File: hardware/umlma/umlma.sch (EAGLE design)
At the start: 13 parts, among them IC1 TINY25, J1 AVRISP6_TP

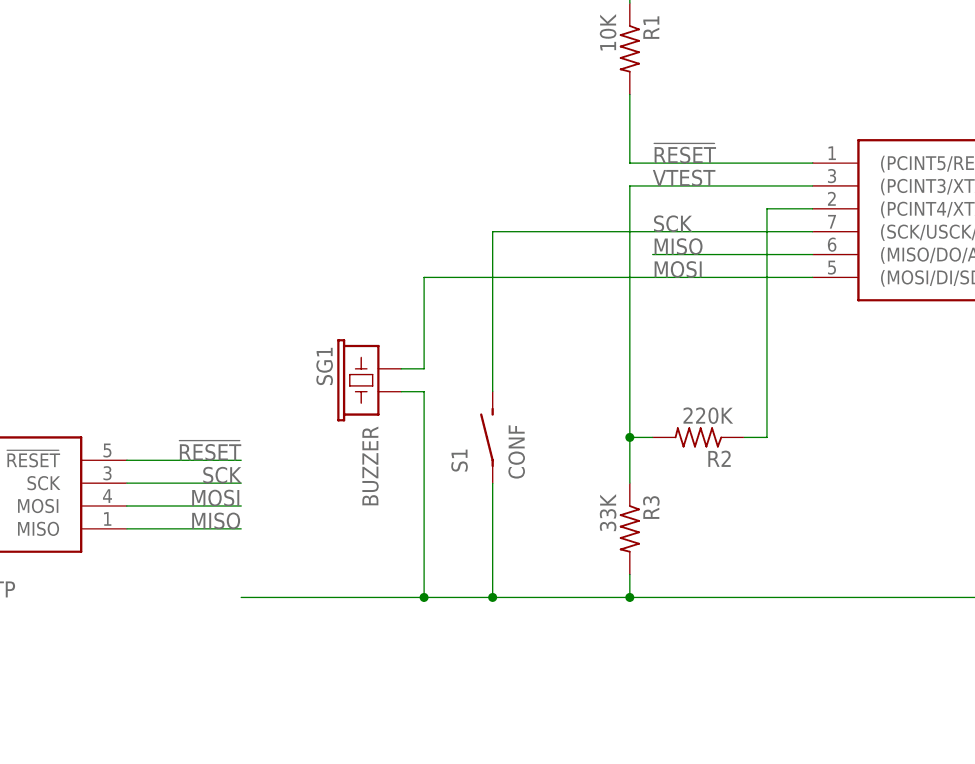
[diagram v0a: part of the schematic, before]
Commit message: revise mcu pin assignments
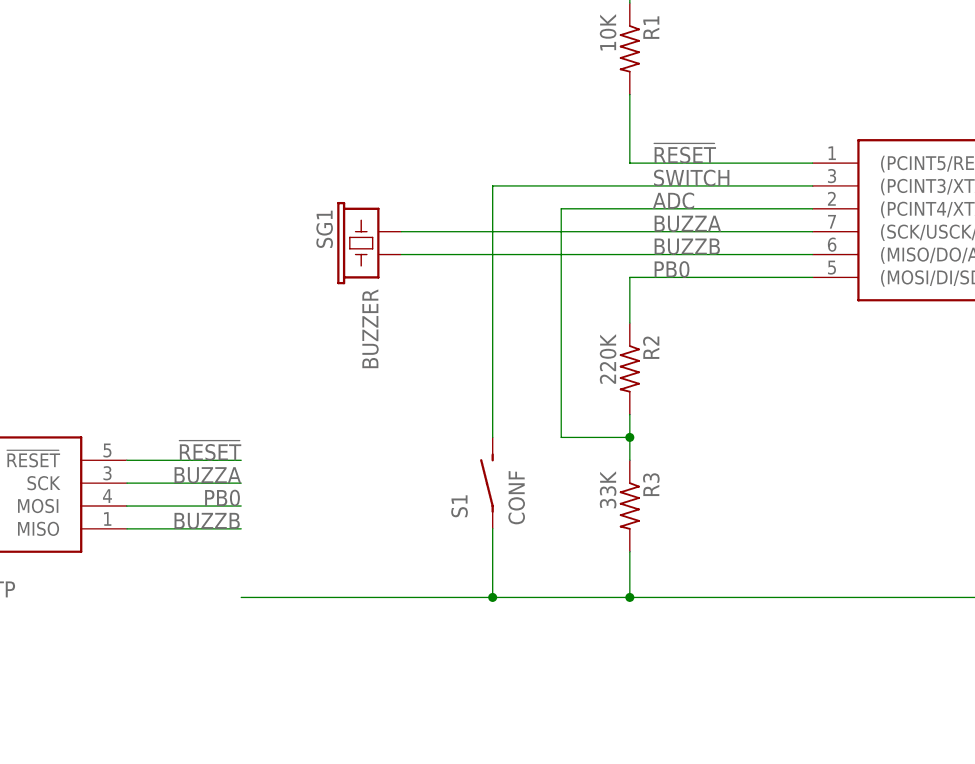
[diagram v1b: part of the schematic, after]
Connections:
- removed net MISO: IC1.(MISO/DO/AIN1/OC0B/OC1A/PCINT1)PB1, J1.MISO
- removed net MOSI: IC1.(MOSI/DI/SDA/AIN0/OC0A/OC1A/AREF/PCINT0)PB0, J1.MOSI, SG1.1
- removed net N$5: IC1.(PCINT4/XTAL2/CLKO/OC1B/ADC2)PB3, R2.1
- removed net SCK: IC1.(SCK/USCK/SCL/ADC1/T0/INT0/PCINT2)PB2, J1.SCK, S1.S
- removed net VTEST: IC1.(PCINT3/XTAL1/CLKI/OC1B/ADC3)PB4, R2.2, R3.1
- new net ADC: IC1.(PCINT4/XTAL2/CLKO/OC1B/ADC2)PB3, R2.2, R3.1
- new net BUZZA: IC1.(SCK/USCK/SCL/ADC1/T0/INT0/PCINT2)PB2, J1.SCK, SG1.1
- new net BUZZB: IC1.(MISO/DO/AIN1/OC0B/OC1A/PCINT1)PB1, J1.MISO, SG1.2
- new net PB0: IC1.(MOSI/DI/SDA/AIN0/OC0A/OC1A/AREF/PCINT0)PB0, J1.MOSI, R2.1
- new net SWITCH: IC1.(PCINT3/XTAL1/CLKI/OC1B/ADC3)PB4, S1.S
- net GND: no longer SG1.2
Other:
- moved on the sheet: R2, R3, S1, SG1
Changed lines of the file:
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@@
 <attribute name="BOM" value="EXCLUDE"/>
-</part>
-<part name="R2" library="rcl" deviceset="R-US_" device="R0603" value="220K">
-<attribute name="PARTNO" value="ERJ-3GEYJ102V"/>
 </part>
 <part name="R3" library="rcl" deviceset="R-US_" device="R0603" value="33K">
@@
 <part name="PAD4" library="wirepad" deviceset="WIREPAD" device="1,6/0,8" value="VCC">
 <attribute name="BOM" value="EXCLUDE"/>
+</part>
+<part name="R2" library="rcl" deviceset="R-US_" device="R0603" value="220K">
+<attribute name="PARTNO" value="ERJ-3GEYJ102V"/>
 </part>
 </parts>
@@
 <instance part="SUPPLY1" gate="GND" x="139.7" y="50.8"/>
 <instance part="P+1" gate="VCC" x="137.16" y="134.62"/>
-<instance part="SG1" gate="G$1" x="71.12" y="83.82" rot="MR270">
-<attribute name="PARTNO" x="71.12" y="83.82" size="1.778" layer="96" rot="MR270" display="off"/>
+<instance part="SG1" gate="G$1" x="71.12" y="99.06" rot="MR270">
+<attribute name="PARTNO" x="71.12" y="99.06" size="1.778" layer="96" rot="MR270" display="off"/>
 </instance>
 <instance part="PAD1" gate="G$1" x="223.52" y="106.68" rot="R180">
@@
 <attribute name="BOM" x="223.52" y="99.06" size="1.778" layer="96" display="off"/>
 </instance>
-<instance part="R2" gate="G$1" x="106.68" y="76.2" rot="R180">
-<attribute name="PARTNO" x="106.68" y="76.2" size="1.778" layer="96" rot="R270" display="off"/>
-</instance>
-<instance part="R3" gate="G$1" x="99.06" y="66.04" rot="R270">
-<attribute name="PARTNO" x="99.06" y="66.04" size="1.778" layer="96" display="off"/>
+<instance part="R3" gate="G$1" x="99.06" y="68.58" rot="R270">
+<attribute name="PARTNO" x="99.06" y="68.58" size="1.778" layer="96" display="off"/>
 </instance>
 <instance part="BAT" gate="G$1" x="215.9" y="86.36" rot="R270">
@@
 <instance part="SUPPLY2" gate="GND" x="10.16" y="55.88"/>
 <instance part="P+2" gate="VCC" x="10.16" y="88.9"/>
-<instance part="S1" gate="G$1" x="83.82" y="76.2" rot="R90"/>
+<instance part="S1" gate="G$1" x="83.82" y="71.12" rot="R90"/>
 <instance part="IC1" gate="1" x="154.94" y="99.06" rot="MR0"/>
 <instance part="PAD3" gate="G$1" x="223.52" y="58.42" rot="R180">
@@
 <instance part="PAD4" gate="G$1" x="223.52" y="127" rot="R180">
 <attribute name="BOM" x="223.52" y="127" size="1.778" layer="96" display="off"/>
+</instance>
+<instance part="R2" gate="G$1" x="99.06" y="83.82" rot="R270">
+<attribute name="PARTNO" x="99.06" y="83.82" size="1.778" layer="96" display="off"/>
 </instance>
 </instances>
@@
 <wire x1="198.12" y1="58.42" x2="203.2" y2="58.42" width="0.1524" layer="91"/>
 <wire x1="139.7" y1="53.34" x2="139.7" y2="58.42" width="0.1524" layer="91"/>
+<wire x1="83.82" y1="58.42" x2="99.06" y2="58.42" width="0.1524" layer="91"/>
 <wire x1="99.06" y1="58.42" x2="139.7" y2="58.42" width="0.1524" layer="91"/>
-<wire x1="76.2" y1="58.42" x2="83.82" y2="58.42" width="0.1524" layer="91"/>
-<wire x1="83.82" y1="58.42" x2="99.06" y2="58.42" width="0.1524" layer="91"/>
-<wire x1="76.2" y1="81.28" x2="73.66" y2="81.28" width="0.1524" layer="91"/>
-<wire x1="76.2" y1="81.28" x2="76.2" y2="58.42" width="0.1524" layer="91"/>
-<wire x1="76.2" y1="58.42" x2="55.88" y2="58.42" width="0.1524" layer="91"/>
-<wire x1="99.06" y1="60.96" x2="99.06" y2="58.42" width="0.1524" layer="91"/>
+<wire x1="83.82" y1="58.42" x2="55.88" y2="58.42" width="0.1524" layer="91"/>
 <junction x="215.9" y="58.42"/>
 <junction x="203.2" y="58.42"/>
 <junction x="139.7" y="58.42"/>
-<junction x="76.2" y="58.42"/>
-<junction x="99.06" y="58.42"/>
 <pinref part="C1" gate="G$1" pin="2"/>
 <pinref part="SUPPLY1" gate="GND" pin="GND"/>
-<pinref part="SG1" gate="G$1" pin="2"/>
-<pinref part="R3" gate="G$1" pin="2"/>
 <pinref part="BAT" gate="G$1" pin="-"/>
 <pinref part="S1" gate="G$1" pin="P"/>
-<wire x1="83.82" y1="71.12" x2="83.82" y2="58.42" width="0.1524" layer="91"/>
+<wire x1="83.82" y1="66.04" x2="83.82" y2="58.42" width="0.1524" layer="91"/>
 <junction x="83.82" y="58.42"/>
 <pinref part="IC1" gate="1" pin="GND"/>
@@
 <junction x="198.12" y="58.42"/>
 <pinref part="PAD3" gate="G$1" pin="P"/>
+<pinref part="R3" gate="G$1" pin="2"/>
+<wire x1="99.06" y1="58.42" x2="99.06" y2="63.5" width="0.1524" layer="91"/>
+<junction x="99.06" y="58.42"/>
 </segment>
 <segment>
@@
 </segment>
 </net>
-<net name="MISO" class="0">
-<segment>
-<wire x1="101.6" y1="96.52" x2="119.38" y2="96.52" width="0.1524" layer="91"/>
-<label x="101.6" y="96.52" size="1.778" layer="95"/>
-<pinref part="IC1" gate="1" pin="(MISO/DO/AIN1/OC0B/OC1A/PCINT1)PB1"/>
-</segment>
-<segment>
-<pinref part="J1" gate="A" pin="MISO"/>
-<wire x1="43.18" y1="66.04" x2="55.88" y2="66.04" width="0.1524" layer="91"/>
-<label x="55.88" y="66.04" size="1.778" layer="95" rot="MR0"/>
-</segment>
-</net>
-<net name="MOSI" class="0">
-<segment>
-<wire x1="76.2" y1="93.98" x2="119.38" y2="93.98" width="0.1524" layer="91"/>
-<wire x1="76.2" y1="83.82" x2="73.66" y2="83.82" width="0.1524" layer="91"/>
-<wire x1="76.2" y1="83.82" x2="76.2" y2="93.98" width="0.1524" layer="91"/>
-<pinref part="SG1" gate="G$1" pin="1"/>
+<net name="PB0" class="0">
+<segment>
+<wire x1="99.06" y1="93.98" x2="119.38" y2="93.98" width="0.1524" layer="91"/>
 <label x="101.6" y="93.98" size="1.778" layer="95"/>
 <pinref part="IC1" gate="1" pin="(MOSI/DI/SDA/AIN0/OC0A/OC1A/AREF/PCINT0)PB0"/>
+<pinref part="R2" gate="G$1" pin="1"/>
+<wire x1="99.06" y1="88.9" x2="99.06" y2="93.98" width="0.1524" layer="91"/>
 </segment>
 <segment>
@@
 <wire x1="43.18" y1="68.58" x2="55.88" y2="68.58" width="0.1524" layer="91"/>
 <label x="55.88" y="68.58" size="1.778" layer="95" rot="MR0"/>
-</segment>
-</net>
-<net name="SCK" class="0">
-<segment>
-<label x="101.6" y="99.06" size="1.778" layer="95"/>
-<pinref part="S1" gate="G$1" pin="S"/>
-<wire x1="83.82" y1="99.06" x2="119.38" y2="99.06" width="0.1524" layer="91"/>
-<wire x1="83.82" y1="81.28" x2="83.82" y2="99.06" width="0.1524" layer="91"/>
-<pinref part="IC1" gate="1" pin="(SCK/USCK/SCL/ADC1/T0/INT0/PCINT2)PB2"/>
-</segment>
-<segment>
-<pinref part="J1" gate="A" pin="SCK"/>
-<wire x1="43.18" y1="71.12" x2="55.88" y2="71.12" width="0.1524" layer="91"/>
-<label x="55.88" y="71.12" size="1.778" layer="95" rot="MR0"/>
 </segment>
 </net>
@@
 </segment>
 </net>
-<net name="VTEST" class="0">
-<segment>
-<wire x1="99.06" y1="71.12" x2="99.06" y2="76.2" width="0.1524" layer="91"/>
-<wire x1="99.06" y1="76.2" x2="99.06" y2="104.14" width="0.1524" layer="91"/>
-<wire x1="99.06" y1="104.14" x2="119.38" y2="104.14" width="0.1524" layer="91"/>
-<wire x1="99.06" y1="76.2" x2="101.6" y2="76.2" width="0.1524" layer="91"/>
-<junction x="99.06" y="76.2"/>
+<net name="SWITCH" class="0">
+<segment>
+<label x="101.6" y="104.14" size="1.778" layer="95"/>
+<pinref part="IC1" gate="1" pin="(PCINT3/XTAL1/CLKI/OC1B/ADC3)PB4"/>
+<pinref part="S1" gate="G$1" pin="S"/>
+<wire x1="83.82" y1="104.14" x2="119.38" y2="104.14" width="0.1524" layer="91"/>
+<wire x1="83.82" y1="76.2" x2="83.82" y2="104.14" width="0.1524" layer="91"/>
+</segment>
+</net>
+<net name="ADC" class="0">
+<segment>
+<pinref part="IC1" gate="1" pin="(PCINT4/XTAL2/CLKO/OC1B/ADC2)PB3"/>
+<wire x1="91.44" y1="101.6" x2="119.38" y2="101.6" width="0.1524" layer="91"/>
+<label x="101.6" y="101.6" size="1.778" layer="95"/>
+<wire x1="91.44" y1="101.6" x2="91.44" y2="76.2" width="0.1524" layer="91"/>
 <pinref part="R3" gate="G$1" pin="1"/>
 <pinref part="R2" gate="G$1" pin="2"/>
-<label x="101.6" y="104.14" size="1.778" layer="95"/>
-<pinref part="IC1" gate="1" pin="(PCINT3/XTAL1/CLKI/OC1B/ADC3)PB4"/>
-</segment>
-</net>
-<net name="N$5" class="0">
-<segment>
-<wire x1="111.76" y1="76.2" x2="114.3" y2="76.2" width="0.1524" layer="91"/>
-<wire x1="114.3" y1="76.2" x2="114.3" y2="101.6" width="0.1524" layer="91"/>
-<wire x1="114.3" y1="101.6" x2="119.38" y2="101.6" width="0.1524" layer="91"/>
-<pinref part="R2" gate="G$1" pin="1"/>
-<pinref part="IC1" gate="1" pin="(PCINT4/XTAL2/CLKO/OC1B/ADC2)PB3"/>
-</segment>
-</net>
+<wire x1="99.06" y1="73.66" x2="99.06" y2="76.2" width="0.1524" layer="91"/>
+<wire x1="99.06" y1="76.2" x2="99.06" y2="78.74" width="0.1524" layer="91"/>
+<wire x1="91.44" y1="76.2" x2="99.06" y2="76.2" width="0.1524" layer="91"/>
+<junction x="99.06" y="76.2"/>
+</segment>
+</net>
+<net name="BUZZA" class="0">
+<segment>
+<label x="101.6" y="99.06" size="1.778" layer="95"/>
+<pinref part="IC1" gate="1" pin="(SCK/USCK/SCL/ADC1/T0/INT0/PCINT2)PB2"/>
+<pinref part="SG1" gate="G$1" pin="1"/>
+<wire x1="73.66" y1="99.06" x2="119.38" y2="99.06" width="0.1524" layer="91"/>
+</segment>
+<segment>
+<pinref part="J1" gate="A" pin="SCK"/>
+<wire x1="43.18" y1="71.12" x2="55.88" y2="71.12" width="0.1524" layer="91"/>
+<label x="55.88" y="71.12" size="1.778" layer="95" rot="MR0"/>
+</segment>
+</net>
+<net name="BUZZB" class="0">
+<segment>
+<label x="101.6" y="96.52" size="1.778" layer="95"/>
+<pinref part="IC1" gate="1" pin="(MISO/DO/AIN1/OC0B/OC1A/PCINT1)PB1"/>
+<pinref part="SG1" gate="G$1" pin="2"/>
+<wire x1="73.66" y1="96.52" x2="119.38" y2="96.52" width="0.1524" layer="91"/>
+</segment>
+<segment>
+<pinref part="J1" gate="A" pin="MISO"/>
+<wire x1="43.18" y1="66.04" x2="55.88" y2="66.04" width="0.1524" layer="91"/>
+<label x="55.88" y="66.04" size="1.778" layer="95" rot="MR0"/>
+</segment>
+</net>

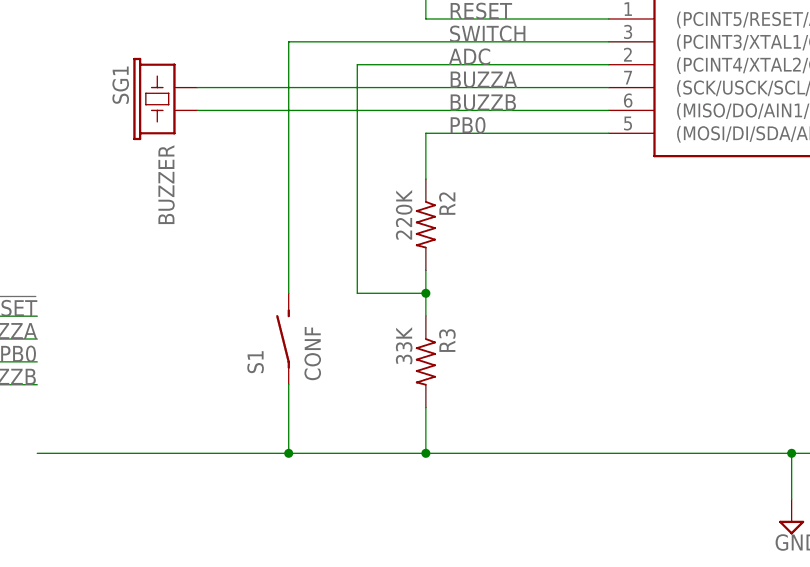
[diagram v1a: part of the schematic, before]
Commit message: updated package to correct labeling error
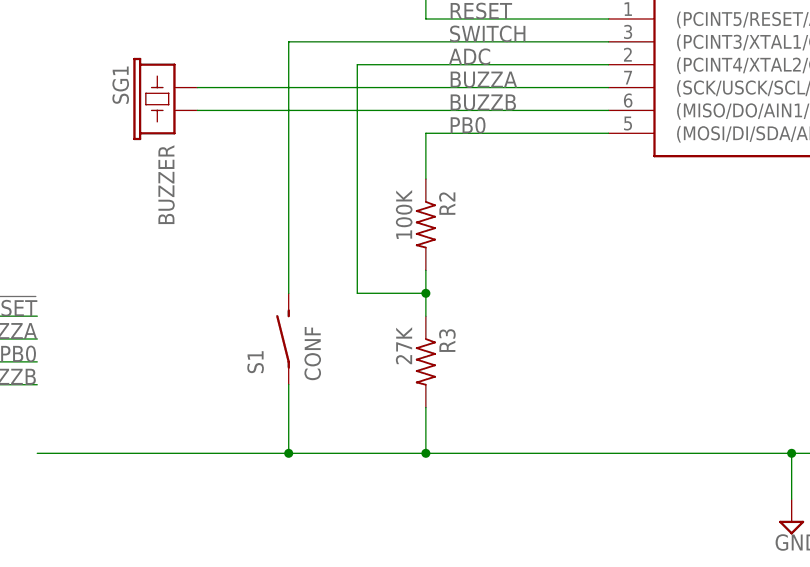
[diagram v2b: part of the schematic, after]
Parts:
- R2: value 220K -> 100K
- R3: value 33K -> 27K
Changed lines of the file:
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@@
 <attribute name="BOM" value="EXCLUDE"/>
 </part>
-<part name="R3" library="rcl" deviceset="R-US_" device="R0603" value="33K">
+<part name="R3" library="rcl" deviceset="R-US_" device="R0603" value="27K">
 <attribute name="PARTNO" value="ERJ-3GEYJ102V"/>
 </part>
@@
 <attribute name="BOM" value="EXCLUDE"/>
 </part>
-<part name="R2" library="rcl" deviceset="R-US_" device="R0603" value="220K">
+<part name="R2" library="rcl" deviceset="R-US_" device="R0603" value="100K">
 <attribute name="PARTNO" value="ERJ-3GEYJ102V"/>
 </part>

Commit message: updates to schematic & layout
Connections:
- net ADC: now also IC1.(PCINT4/XTAL2/CLKO/OC1B/ADC3)PB3; no longer IC1.(PCINT4/XTAL2/CLKO/OC1B/ADC2)PB3
- net SWITCH: now also IC1.(PCINT3/XTAL1/CLKI/OC1B/ADC2)PB4; no longer IC1.(PCINT3/XTAL1/CLKI/OC1B/ADC3)PB4
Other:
- note added: "Use 1.1V internal reference"
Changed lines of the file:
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@@
 <layer number="110" name="fp0" color="7" fill="1" visible="no" active="yes"/>
 <layer number="111" name="LPC17xx" color="7" fill="1" visible="no" active="yes"/>
+<layer number="112" name="tSilk" color="7" fill="1" visible="yes" active="yes"/>
 <layer number="113" name="IDFDebug" color="4" fill="1" visible="no" active="yes"/>
+<layer number="114" name="Badge_Outline" color="7" fill="1" visible="yes" active="yes"/>
+<layer number="115" name="ReferenceISLANDS" color="7" fill="1" visible="yes" active="yes"/>
 <layer number="116" name="Patch_BOT" color="9" fill="4" visible="yes" active="yes"/>
+<layer number="118" name="Rect_Pads" color="7" fill="1" visible="yes" active="yes"/>
 <layer number="121" name="_tsilk" color="7" fill="1" visible="yes" active="yes"/>
 <layer number="122" name="_bsilk" color="7" fill="1" visible="yes" active="yes"/>
@@
 <text x="160.02" y="25.4" size="2.54" layer="94">Ultra Micro Lost Model Alarm</text>
 <text x="231.14" y="25.4" size="2.54" layer="94">R0.4</text>
+<text x="104.14" y="76.2" size="1.778" layer="97">Use 1.1V internal reference</text>
 </plain>
 <instances>
@@
 <instance part="SUPPLY2" gate="GND" x="10.16" y="55.88"/>
 <instance part="P+2" gate="VCC" x="10.16" y="88.9"/>
-<instance part="S1" gate="G$1" x="83.82" y="71.12" rot="R90"/>
+<instance part="S1" gate="S1" x="83.82" y="71.12" rot="R90"/>
 <instance part="IC1" gate="1" x="154.94" y="99.06" rot="MR0"/>
 <instance part="PAD3" gate="G$1" x="223.52" y="58.42" rot="R180">
@@
 <pinref part="SUPPLY1" gate="GND" pin="GND"/>
 <pinref part="BAT" gate="G$1" pin="-"/>
-<pinref part="S1" gate="G$1" pin="P"/>
+<pinref part="S1" gate="S1" pin="P"/>
 <wire x1="83.82" y1="66.04" x2="83.82" y2="58.42" width="0.1524" layer="91"/>
 <junction x="83.82" y="58.42"/>
@@
 <segment>
 <label x="101.6" y="104.14" size="1.778" layer="95"/>
-<pinref part="IC1" gate="1" pin="(PCINT3/XTAL1/CLKI/OC1B/ADC3)PB4"/>
-<pinref part="S1" gate="G$1" pin="S"/>
+<pinref part="IC1" gate="1" pin="(PCINT3/XTAL1/CLKI/OC1B/ADC2)PB4"/>
+<pinref part="S1" gate="S1" pin="S"/>
 <wire x1="83.82" y1="104.14" x2="119.38" y2="104.14" width="0.1524" layer="91"/>
 <wire x1="83.82" y1="76.2" x2="83.82" y2="104.14" width="0.1524" layer="91"/>
@@
 <net name="ADC" class="0">
 <segment>
-<pinref part="IC1" gate="1" pin="(PCINT4/XTAL2/CLKO/OC1B/ADC2)PB3"/>
+<pinref part="IC1" gate="1" pin="(PCINT4/XTAL2/CLKO/OC1B/ADC3)PB3"/>
 <wire x1="91.44" y1="101.6" x2="119.38" y2="101.6" width="0.1524" layer="91"/>
 <label x="101.6" y="101.6" size="1.778" layer="95"/>

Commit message: updated layout, silk, gerbers, zip
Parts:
- added U$1: BTLOGO-LOGO-SM, bt:BTLOGO-LOGO-SM
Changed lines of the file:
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@@
 <attribute name="PARTNO" value="ERJ-3GEYJ102V"/>
 </part>
+<part name="U$1" library="bt" deviceset="BTLOGO" device="-LOGO-SM"/>
 </parts>
 <sheets>
@@
 <attribute name="PARTNO" x="99.06" y="83.82" size="1.778" layer="96" display="off"/>
 </instance>
+<instance part="U$1" gate="G$1" x="5.08" y="5.08"/>
 </instances>
 <busses>
